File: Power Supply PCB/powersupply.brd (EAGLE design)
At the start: 87.3 x 63.5 mm, 23 parts

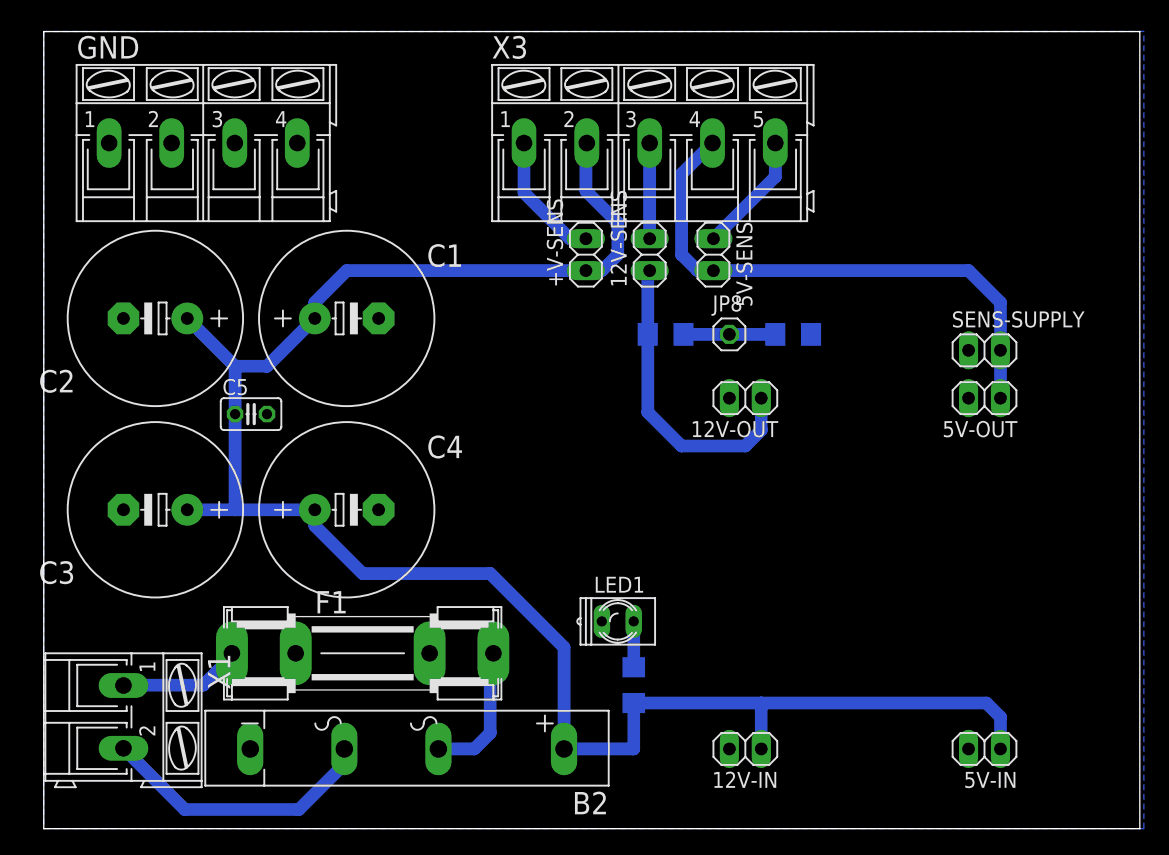
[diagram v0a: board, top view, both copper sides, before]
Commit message: Add light power supply board
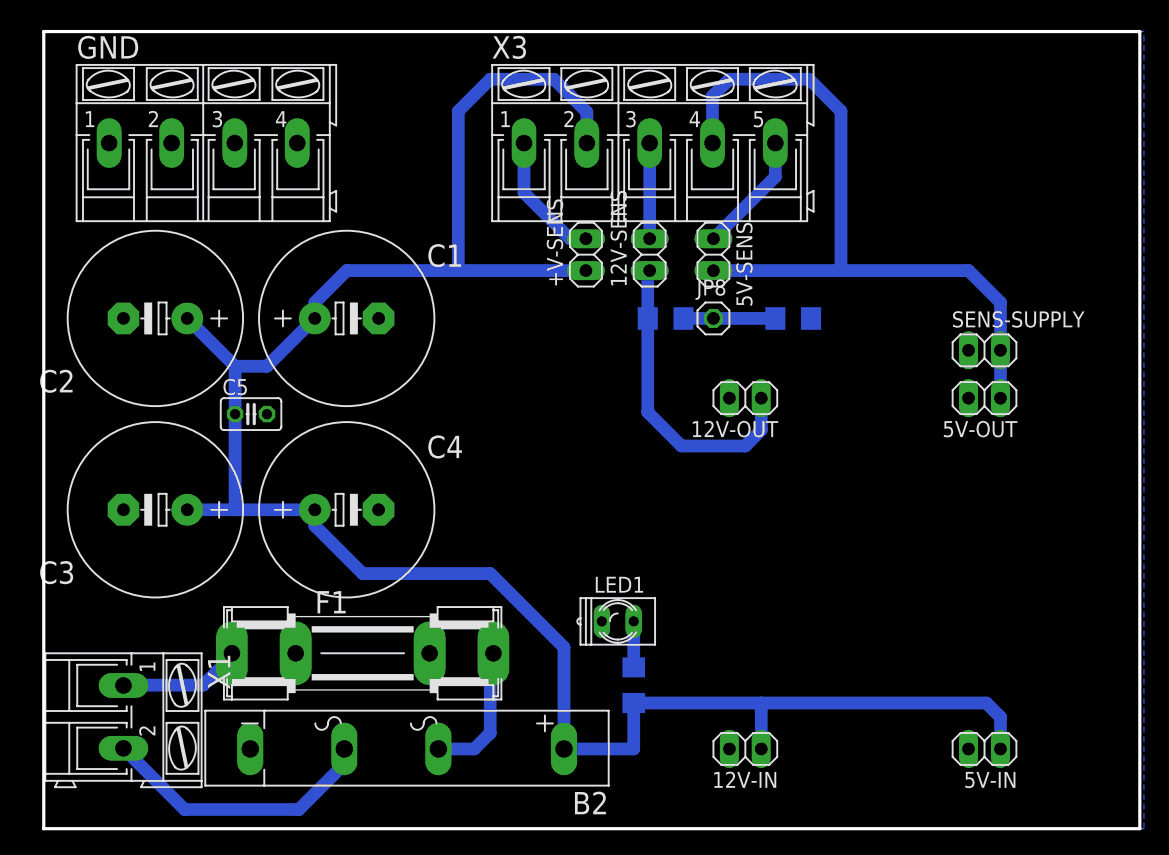
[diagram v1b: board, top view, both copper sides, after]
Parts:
- moved JP8 1.80 mm to (53.3, 40.6)
- moved R1 1.27 mm to (49.5, 40.6)
- moved R2 1.27 mm to (59.7, 40.6)
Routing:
- net +5V: track 44.5 -> 59.8 mm
- net V+: track 150.2 -> 164.7 mm
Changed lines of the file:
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@@
 <drawing>
 <settings>
-<setting alwaysvectorfont="yes"/>
+<setting alwaysvectorfont="no"/>
 <setting verticaltext="up"/>
 </settings>
-<grid distance="50" unitdist="mil" unit="mil" style="lines" multiple="1" display="no" altdistance="5" altunitdist="mil" altunit="mil"/>
+<grid distance="50" unitdist="mil" unit="mm" style="lines" multiple="1" display="no" altdistance="5" altunitdist="mil" altunit="mil"/>
 <layers>
 <layer number="1" name="Top" color="4" fill="1" visible="yes" active="yes"/>
@@
 </layers>
 <board>
+<fusionsync huburn="a.cGVyc29uYWw6dWUyZGM4MWM3" projecturn="a.cGVyc29uYWw6dWUyZGM4MWM3I0QyMDE4MDQxMzEyNzQyMzUyNg" f3durn="urn:adsk.wipprod:dm.lineage:CiXKUrinQ5C1w3OZ4GbuDA" pcbguid="0aeefe17-c1ae-4475-b27b-de719b40e365" lastpulledtime="2018-04-22T17:52:54Z" lastsyncedchangeguid="89d808e5-60cc-09e5-48b8-2e7406ad3e9a"/>
 <plain>
-<wire x1="0" y1="0" x2="87.3" y2="0" width="0" layer="20"/>
-<wire x1="87.3" y1="0" x2="87.3" y2="63.49" width="0" layer="20"/>
-<wire x1="87.3" y1="63.49" x2="0" y2="63.49" width="0" layer="20"/>
-<wire x1="0" y1="63.49" x2="0" y2="0" width="0" layer="20"/>
+<wire x1="0" y1="0" x2="87.3" y2="0" width="0.254" layer="20"/>
+<wire x1="87.3" y1="0" x2="87.3" y2="63.49" width="0.254" layer="20"/>
+<wire x1="87.3" y1="63.49" x2="0" y2="63.49" width="0.254" layer="20"/>
+<wire x1="0" y1="63.49" x2="0" y2="0" width="0.254" layer="20"/>
 </plain>
 <attributes>
@@
 <param name="mtCopper" value="0.035mm 0.035mm 0.035mm 0.035mm 0.035mm 0.035mm 0.035mm 0.035mm 0.035mm 0.035mm 0.035mm 0.035mm 0.035mm 0.035mm 0.035mm 0.035mm"/>
 <param name="mtIsolate" value="1.5mm 0.15mm 0.2mm 0.15mm 0.2mm 0.15mm 0.2mm 0.15mm 0.2mm 0.15mm 0.2mm 0.15mm 0.2mm 0.15mm 0.2mm"/>
-<param name="mdWireWire" value="1mm"/>
-<param name="mdWirePad" value="1mm"/>
+<param name="mdWireWire" value="1.4mm"/>
+<param name="mdWirePad" value="1.4mm"/>
 <param name="mdWireVia" value="6mil"/>
 <param name="mdPadPad" value="6mil"/>
@@
 <element name="5V-IN" library="pinhead" library_urn="urn:adsk.eagle:library:325" package="1X02" package3d_urn="urn:adsk.eagle:package:22435/2" value="" x="74.93" y="6.35" rot="R180"/>
 <element name="5V-OUT" library="pinhead" library_urn="urn:adsk.eagle:library:325" package="1X02" package3d_urn="urn:adsk.eagle:package:22435/2" value="" x="74.93" y="34.29" rot="R180"/>
-<element name="JP8" library="pinhead" library_urn="urn:adsk.eagle:library:325" package="1X01" package3d_urn="urn:adsk.eagle:package:22485/2" value="" x="54.61" y="39.37"/>
+<element name="JP8" library="pinhead" library_urn="urn:adsk.eagle:library:325" package="1X01" package3d_urn="urn:adsk.eagle:package:22485/2" value="" x="53.34" y="40.64"/>
 <element name="LED1" library="led" library_urn="urn:adsk.eagle:library:259" package="Q62902-B152" package3d_urn="urn:adsk.eagle:package:15803/1" value="" x="45.72" y="16.51"/>
-<element name="R1" library="rcl" library_urn="urn:adsk.eagle:library:334" package="R1206" package3d_urn="urn:adsk.eagle:package:23540/2" value="" x="49.53" y="39.37" rot="MR0">
-<attribute name="SPICEPREFIX" value="R" x="49.53" y="39.37" size="1.778" layer="28" rot="MR0" display="off"/>
-</element>
-<element name="R2" library="rcl" library_urn="urn:adsk.eagle:library:334" package="R1206" package3d_urn="urn:adsk.eagle:package:23540/2" value="" x="59.69" y="39.37" rot="MR0">
-<attribute name="SPICEPREFIX" value="R" x="59.69" y="39.37" size="1.778" layer="28" rot="MR0" display="off"/>
+<element name="R1" library="rcl" library_urn="urn:adsk.eagle:library:334" package="R1206" package3d_urn="urn:adsk.eagle:package:23540/2" value="" x="49.53" y="40.64" rot="MR0">
+<attribute name="SPICEPREFIX" value="R" x="49.53" y="40.64" size="1.778" layer="28" rot="MR0" display="off"/>
+</element>
+<element name="R2" library="rcl" library_urn="urn:adsk.eagle:library:334" package="R1206" package3d_urn="urn:adsk.eagle:package:23540/2" value="" x="59.69" y="40.64" rot="MR0">
+<attribute name="SPICEPREFIX" value="R" x="59.69" y="40.64" size="1.778" layer="28" rot="MR0" display="off"/>
 </element>
 <element name="R3" library="rcl" library_urn="urn:adsk.eagle:library:334" package="R1206" package3d_urn="urn:adsk.eagle:package:23540/2" value="" x="46.99" y="11.43" rot="MR270">
@@
 <wire x1="25.4" y1="20.32" x2="21.59" y2="24.13" width="1.016" layer="16"/>
 <wire x1="21.59" y1="24.13" x2="21.59" y2="25.4" width="1.016" layer="16"/>
-<wire x1="43.18" y1="44.45" x2="24.13" y2="44.45" width="1.016" layer="16"/>
+<wire x1="43.18" y1="44.45" x2="33.02" y2="44.45" width="1.016" layer="16"/>
+<wire x1="33.02" y1="44.45" x2="24.13" y2="44.45" width="1.016" layer="16"/>
 <wire x1="24.13" y1="44.45" x2="21.59" y2="41.91" width="1.016" layer="16"/>
 <wire x1="21.59" y1="41.91" x2="21.59" y2="40.64" width="1.016" layer="16"/>
-<wire x1="43.18" y1="44.45" x2="44.45" y2="44.45" width="1.016" layer="16"/>
-<wire x1="44.45" y1="44.45" x2="45.72" y2="45.72" width="1.016" layer="16"/>
-<wire x1="45.72" y1="45.72" x2="45.72" y2="48.26" width="1.016" layer="16"/>
-<wire x1="45.72" y1="48.26" x2="43.18" y2="50.8" width="1.016" layer="16"/>
-<wire x1="43.18" y1="50.8" x2="43.18" y2="54.5338" width="1.016" layer="16"/>
-<wire x1="43.18" y1="54.5338" x2="43.2562" y2="54.61" width="1.016" layer="16"/>
 <wire x1="46.99" y1="10.008" x2="57.15" y2="10.008" width="1.016" layer="16"/>
 <wire x1="57.15" y1="6.35" x2="57.15" y2="10.008" width="1.016" layer="16"/>
@@
 <wire x1="76.2" y1="8.89" x2="76.2" y2="6.35" width="1.016" layer="16"/>
 <wire x1="57.15" y1="10.008" x2="75.082" y2="10.008" width="1.016" layer="16"/>
+<wire x1="43.2562" y1="54.61" x2="43.2562" y2="57.0738" width="1.016" layer="16"/>
+<wire x1="43.2562" y1="57.0738" x2="40.64" y2="59.69" width="1.016" layer="16"/>
+<wire x1="40.64" y1="59.69" x2="35.56" y2="59.69" width="1.016" layer="16"/>
+<wire x1="35.56" y1="59.69" x2="33.02" y2="57.15" width="1.016" layer="16"/>
+<wire x1="33.02" y1="57.15" x2="33.02" y2="44.45" width="1.016" layer="16"/>
 </signal>
 <signal name="GND">
@@
 <contactref element="5V-OUT" pad="1"/>
 <contactref element="SENS-SUPPLY" pad="2"/>
-<wire x1="53.2638" y1="54.61" x2="50.8" y2="52.1462" width="1.016" layer="16"/>
-<wire x1="50.8" y1="52.1462" x2="50.8" y2="45.72" width="1.016" layer="16"/>
-<wire x1="50.8" y1="45.72" x2="52.07" y2="44.45" width="1.016" layer="16"/>
-<wire x1="52.07" y1="44.45" x2="53.34" y2="44.45" width="1.016" layer="16"/>
-<wire x1="53.34" y1="44.45" x2="73.66" y2="44.45" width="1.016" layer="16"/>
+<wire x1="53.34" y1="44.45" x2="63.5" y2="44.45" width="1.016" layer="16"/>
+<wire x1="63.5" y1="44.45" x2="73.66" y2="44.45" width="1.016" layer="16"/>
 <wire x1="73.66" y1="44.45" x2="76.2" y2="41.91" width="1.016" layer="16"/>
 <wire x1="76.2" y1="41.91" x2="76.2" y2="38.1" width="1.016" layer="16"/>
 <wire x1="76.2" y1="34.29" x2="76.2" y2="38.1" width="1.016" layer="16"/>
+<wire x1="53.2638" y1="54.61" x2="53.2638" y2="58.3438" width="1.016" layer="16"/>
+<wire x1="53.2638" y1="58.3438" x2="54.61" y2="59.69" width="1.016" layer="16"/>
+<wire x1="54.61" y1="59.69" x2="60.96" y2="59.69" width="1.016" layer="16"/>
+<wire x1="60.96" y1="59.69" x2="63.5" y2="57.15" width="1.016" layer="16"/>
+<wire x1="63.5" y1="57.15" x2="63.5" y2="44.45" width="1.016" layer="16"/>
 </signal>
 <signal name="+12V">
@@
 <contactref element="12V-OUT" pad="1"/>
 <contactref element="R1" pad="2"/>
-<wire x1="48.108" y1="39.37" x2="48.108" y2="44.298" width="1.016" layer="16"/>
+<wire x1="48.108" y1="40.64" x2="48.108" y2="44.298" width="1.016" layer="16"/>
 <wire x1="48.108" y1="44.298" x2="48.26" y2="44.45" width="1.016" layer="16"/>
 <wire x1="57.15" y1="34.29" x2="57.15" y2="31.75" width="1.016" layer="16"/>
 <wire x1="57.15" y1="31.75" x2="55.88" y2="30.48" width="1.016" layer="16"/>
 <wire x1="55.88" y1="30.48" x2="50.8" y2="30.48" width="1.016" layer="16"/>
-<wire x1="48.108" y1="33.172" x2="48.108" y2="39.37" width="1.016" layer="16"/>
+<wire x1="48.108" y1="33.172" x2="48.108" y2="40.64" width="1.016" layer="16"/>
 <wire x1="50.8" y1="30.48" x2="48.108" y2="33.172" width="1.016" layer="16"/>
 </signal>
@@
 <contactref element="R1" pad="1"/>
 <contactref element="R2" pad="2"/>
-<wire x1="50.952" y1="39.37" x2="54.61" y2="39.37" width="1.016" layer="16"/>
-<wire x1="54.61" y1="39.37" x2="58.268" y2="39.37" width="1.016" layer="16"/>
+<wire x1="50.952" y1="40.64" x2="53.34" y2="40.64" width="1.016" layer="16"/>
+<wire x1="53.34" y1="40.64" x2="58.268" y2="40.64" width="1.016" layer="16"/>
 </signal>
 </signals>
@@
 </note>
 <note version="8.3" severity="warning">
+Since Version 8.3, EAGLE supports Fusion synchronisation.
+This feature will not be available in this version and saving
+the document will break the link to the Fusion PCB feature.
+</note>
+<note version="8.3" severity="warning">
